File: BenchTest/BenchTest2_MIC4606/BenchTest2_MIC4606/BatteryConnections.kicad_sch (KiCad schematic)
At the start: 5 parts, among them J6 Conn_01x01_Socket, J7 Conn_01x01_Socket

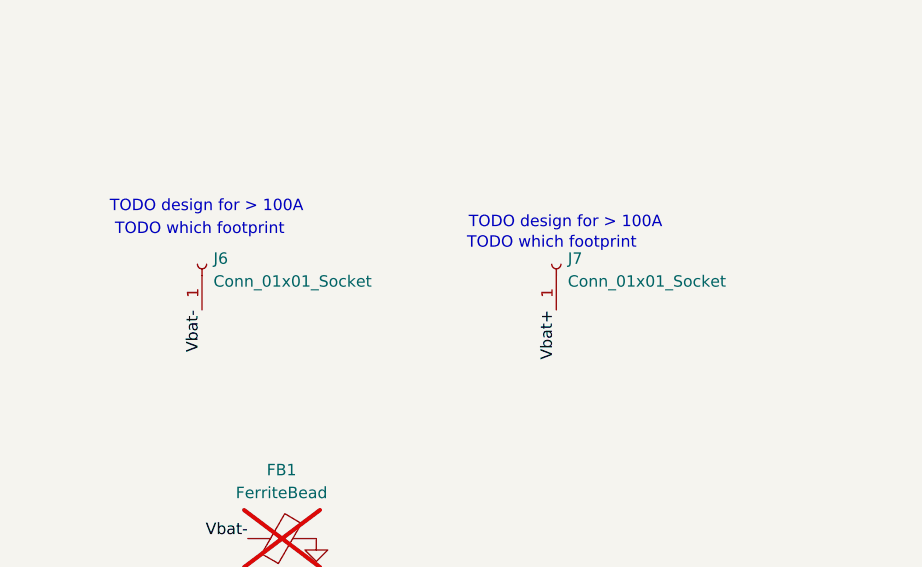
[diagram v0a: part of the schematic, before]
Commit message: Assigned HP Footprints
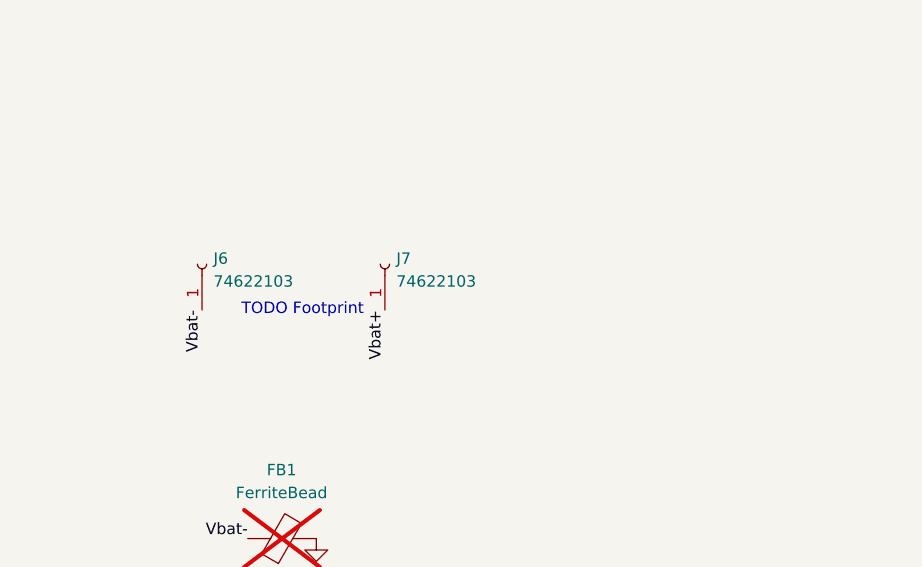
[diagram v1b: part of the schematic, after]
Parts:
- J6, J7: value Conn_01x01_Socket -> 74622103
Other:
- note added: "TODO Footprint"
- note removed: "TODO design for > 100A"
- note removed: "TODO which footprint"
- moved on the sheet: J7
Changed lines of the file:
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@@
 		)
 	)
-	(text "TODO design for > 100A"
+	(text "TODO Footprint"
 		(exclude_from_sim no)
-		(at 145.796 91.948 0)
-		(effects
-			(font
-				(size 1.27 1.27)
-			)
-		)
-	)
-	(text "TODO which footprint"
-		(exclude_from_sim no)
-		(at 105.156 92.71 0)
-		(effects
-			(font
-				(size 1.27 1.27)
-			)
-		)
-	)
-	(text "TODO which footprint"
-		(exclude_from_sim no)
-		(at 144.272 94.234 0)
-		(effects
-			(font
-				(size 1.27 1.27)
-			)
-		)
-	)
-	(text "TODO design for > 100A"
-		(exclude_from_sim no)
-		(at 105.918 90.17 0)
+		(at 116.586 101.6 0)
 		(effects
 			(font
@@
 	)
 	(label "Vbat+"
-		(at 144.78 101.6 270)
+		(at 125.73 101.6 270)
 		(effects
 			(font
@@
 			)
 		)
-		(property "Value" "Conn_01x01_Socket"
+		(property "Value" "74622103"
 			(at 106.68 98.4249 90)
 			(effects
@@
 			)
 		)
-		(property "Description" "Generic connector, single row, 01x01, script generated"
+		(property "Description" "74622103"
 			(at 105.41 96.52 0)
 			(effects
@@
 	(symbol
 		(lib_id "Connector:Conn_01x01_Socket")
-		(at 144.78 96.52 90)
+		(at 125.73 96.52 90)
 		(unit 1)
 		(exclude_from_sim no)
@@
 		(fields_autoplaced yes)
 		(property "Reference" "J7"
-			(at 146.05 95.8849 90)
-			(effects
-				(font
-					(size 1.27 1.27)
-				)
-				(justify right)
-			)
-		)
-		(property "Value" "Conn_01x01_Socket"
-			(at 146.05 98.4249 90)
+			(at 127 95.8849 90)
+			(effects
+				(font
+					(size 1.27 1.27)
+				)
+				(justify right)
+			)
+		)
+		(property "Value" "74622103"
+			(at 127 98.4249 90)
 			(effects
 				(font
@@
 		)
 		(property "Footprint" ""
-			(at 144.78 96.52 0)
+			(at 125.73 96.52 0)
 			(effects
 				(font
@@
 		)
 		(property "Datasheet" "~"
-			(at 144.78 96.52 0)
-			(effects
-				(font
-					(size 1.27 1.27)
-				)
-				(hide yes)
-			)
-		)
-		(property "Description" "Generic connector, single row, 01x01, script generated"
-			(at 144.78 96.52 0)
-			(effects
-				(font
+			(at 125.73 96.52 0)
+			(effects
+				(font
+					(size 1.27 1.27)
+				)
+				(hide yes)
+			)
+		)
+		(property "Description" "74622103"
+			(at 125.73 96.52 0)
+			(effects
+				(font

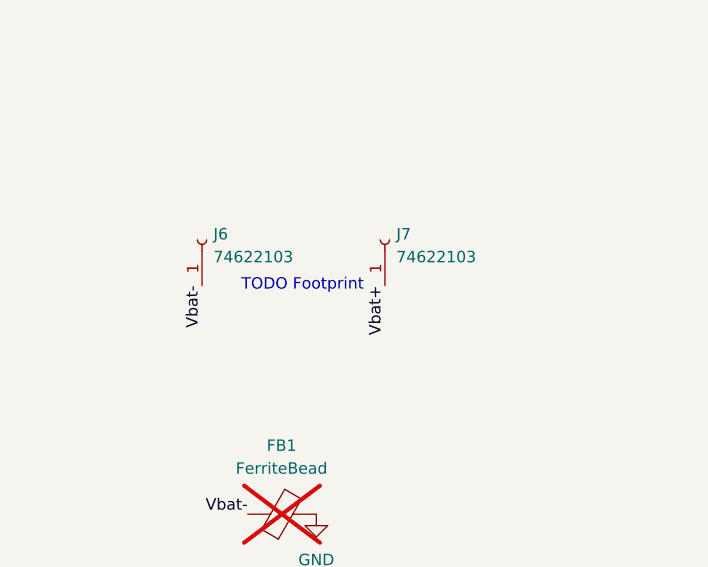
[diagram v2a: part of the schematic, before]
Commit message: Connector Footprints Assigned
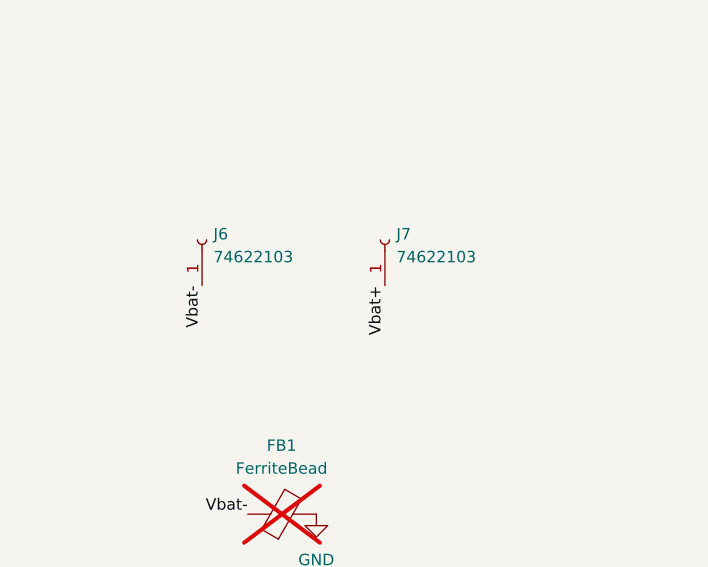
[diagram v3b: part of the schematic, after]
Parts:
- J6, J7: footprint (none) -> Library:WP-RAFE_74622103
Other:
- note removed: "TODO Footprint"
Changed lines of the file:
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@@
-		)
-	)
-	(text "TODO Footprint"
-		(exclude_from_sim no)
-		(at 116.586 101.6 0)
-		(effects
-			(font
-				(size 1.27 1.27)
-			)
 		)
 	)
@@
 			)
 		)
-		(property "Footprint" ""
+		(property "Footprint" "Library:WP-RAFE_74622103"
 			(at 105.41 96.52 0)
 			(effects
@@
 			)
 		)
-		(property "Footprint" ""
+		(property "Footprint" "Library:WP-RAFE_74622103"
 			(at 125.73 96.52 0)
 			(effects
